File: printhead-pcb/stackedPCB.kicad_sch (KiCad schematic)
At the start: 5 parts, among them J3 Conn_02x08_Row_Letter_Last

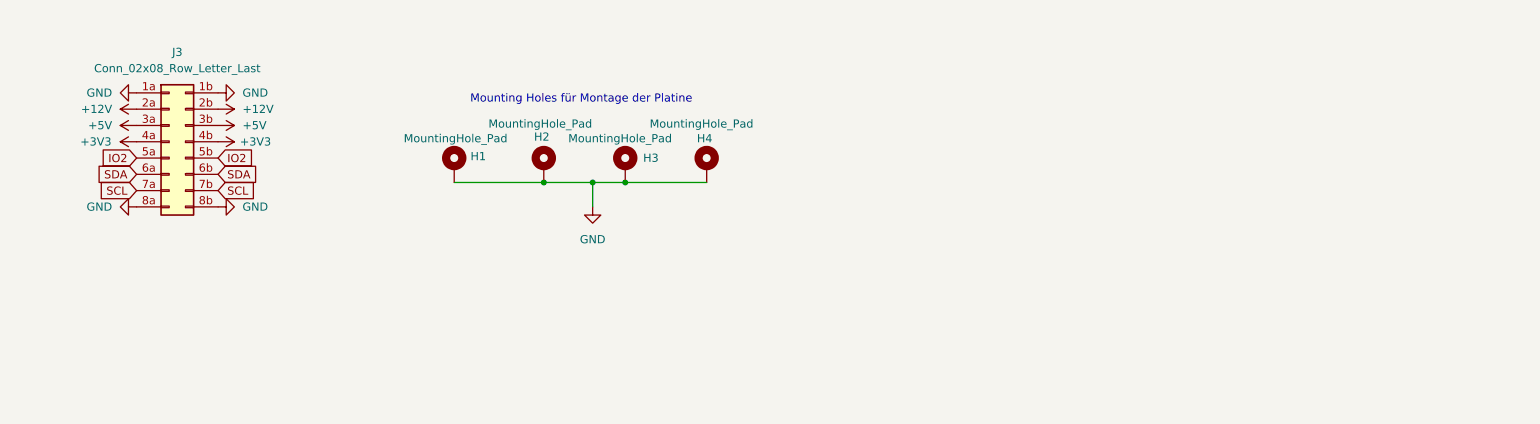
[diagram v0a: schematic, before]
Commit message: made first pcb design of module 1 with components on front and back
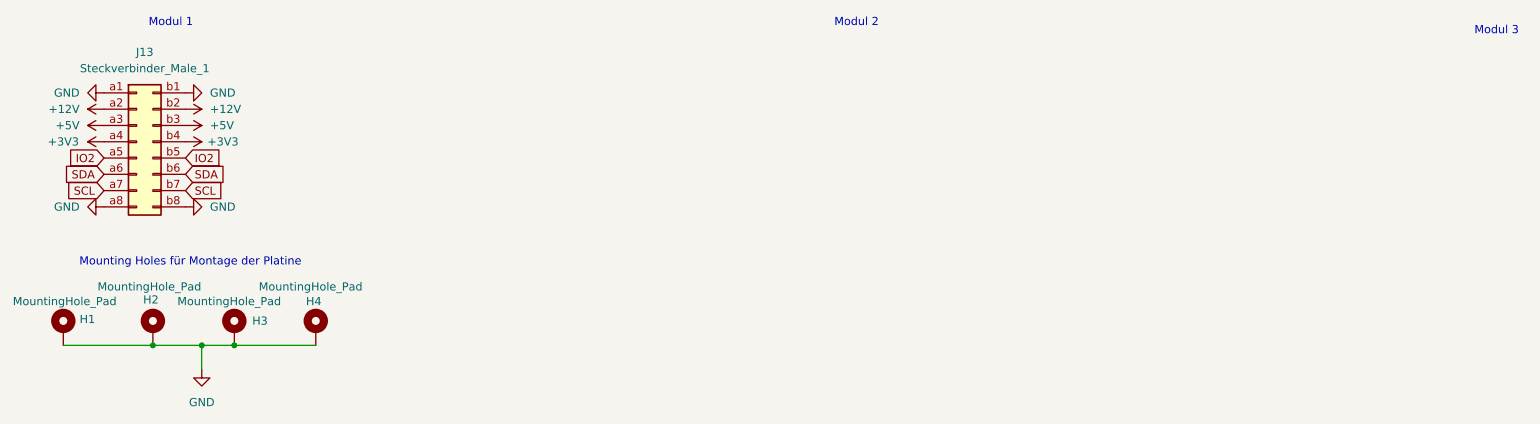
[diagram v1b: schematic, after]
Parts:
- removed J3: Conn_02x08_Row_Letter_Last, symbol Connector_Generic:Conn_02x08_Row_Letter_Last
- added J13: Steckverbinder_Male_1, CustomFotLibByJan:BF100-16-A-D-1-0640-L-C, symbol Connector_Generic:Conn_02x08_Row_Letter_First
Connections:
- net +12V: now also J13.a2 (Pin_a2), J13.b2 (Pin_b2)
- net +3V3: now also J13.a4 (Pin_a4), J13.b4 (Pin_b4)
- net +5V: now also J13.a3 (Pin_a3), J13.b3 (Pin_b3)
- net GND: now also J13.a1 (Pin_a1), J13.a8 (Pin_a8), J13.b1 (Pin_b1), J13.b8 (Pin_b8)
- net IO2: now also J13.a5 (Pin_a5), J13.b5 (Pin_b5)
- net SCL: now also J13.a7 (Pin_a7), J13.b7 (Pin_b7)
- net SDA: now also J13.a6 (Pin_a6), J13.b6 (Pin_b6)
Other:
- note added: "Modul 1"
- note added: "Modul 2"
- note added: "Modul 3"
- moved on the sheet: H1, H2, H3, H4

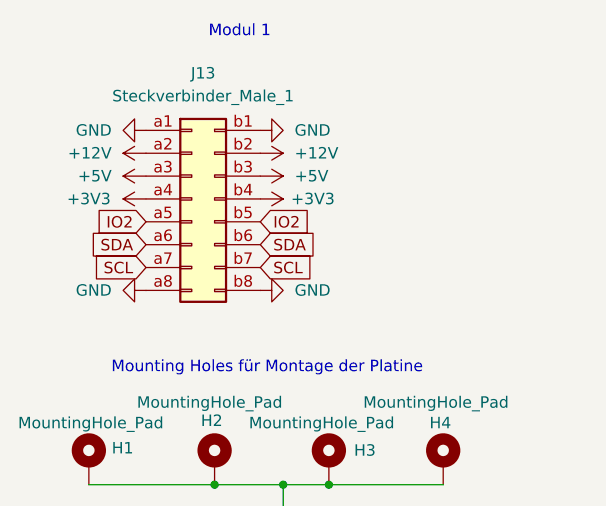
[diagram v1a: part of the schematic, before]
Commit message: alle module mal grob gemacht, beim ersten noch den gpio hinzugefuegt, leider nicht auf einer layerseite untergebracht
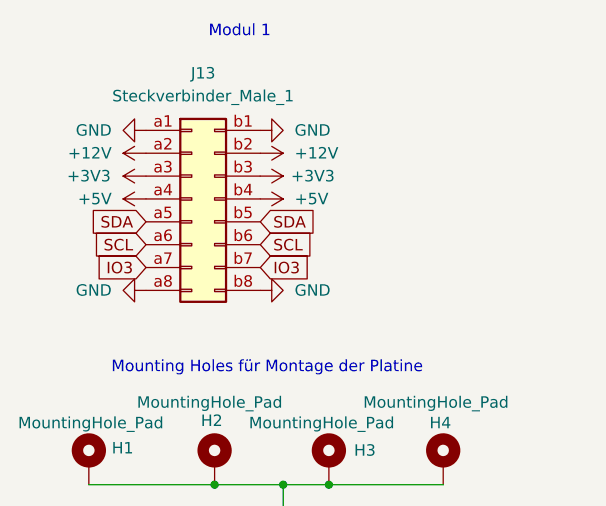
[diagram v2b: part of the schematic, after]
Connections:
- net IO2 is gone; now on net SDA: J13.a5 (Pin_a5), J13.b5 (Pin_b5)
- net +3V3: now also J13.a3 (Pin_a3), J13.b3 (Pin_b3); no longer J13.a4 (Pin_a4), J13.b4 (Pin_b4)
- net +5V: now also J13.a4 (Pin_a4), J13.b4 (Pin_b4); no longer J13.a3 (Pin_a3), J13.b3 (Pin_b3)
- net SCL: now also J13.a6 (Pin_a6), J13.b6 (Pin_b6); no longer J13.a7 (Pin_a7), J13.b7 (Pin_b7)
- net SDA: no longer J13.a6 (Pin_a6), J13.b6 (Pin_b6)
- new net IO3: J13.a7 (Pin_a7), J13.b7 (Pin_b7)

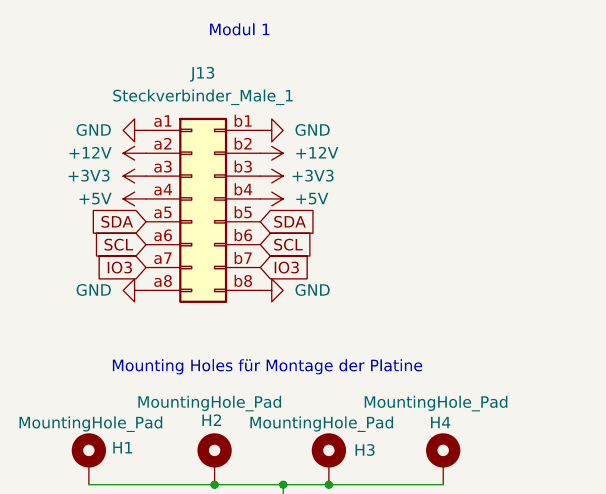
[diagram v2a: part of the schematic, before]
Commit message: working, good version with one layer and equally long signal routes, thicker traces and fitting text
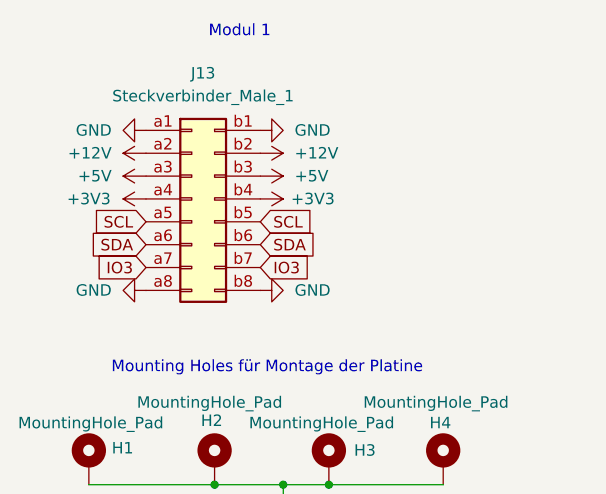
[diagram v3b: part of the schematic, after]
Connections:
- net +3V3: now also J13.a4 (Pin_a4), J13.b4 (Pin_b4); no longer J13.a3 (Pin_a3), J13.b3 (Pin_b3)
- net +5V: now also J13.a3 (Pin_a3), J13.b3 (Pin_b3); no longer J13.a4 (Pin_a4), J13.b4 (Pin_b4)
- net SCL: now also J13.a5 (Pin_a5), J13.b5 (Pin_b5); no longer J13.a6 (Pin_a6), J13.b6 (Pin_b6)
- net SDA: now also J13.a6 (Pin_a6), J13.b6 (Pin_b6); no longer J13.a5 (Pin_a5), J13.b5 (Pin_b5)

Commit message: prepared second module for tomorrow
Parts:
- added H5, H6, H7, H8: MountingHole_Pad, MountingHole:MountingHole_2.2mm_M2_Pad_TopBottom, symbol Mechanical:MountingHole_Pad
- added J14: Steckverbinder_Male_2, CustomFotLibByJan:BF100-16-A-D-1-0640-L-C, symbol Connector_Generic:Conn_02x08_Row_Letter_First
- added J15: Steckverbinder_Female_2, CustomFotLibByJan:BF100-16-A-D-1-0640-L-C, symbol Connector_Generic:Conn_02x08_Row_Letter_First
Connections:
- net +12V: now also J14.a2 (Pin_a2), J14.b2 (Pin_b2), J15.a2 (Pin_a2), J15.b2 (Pin_b2)
- net +3V3: now also J14.a4 (Pin_a4), J14.b4 (Pin_b4), J15.a4 (Pin_a4), J15.b4 (Pin_b4)
- net +5V: now also J14.a3 (Pin_a3), J14.b3 (Pin_b3), J15.a3 (Pin_a3), J15.b3 (Pin_b3)
- net GND: now also H5.1, H6.1, H7.1, H8.1, J14.a1 (Pin_a1), J14.a8 (Pin_a8), J14.b1 (Pin_b1), J14.b8 (Pin_b8), J15.a1 (Pin_a1), J15.a8 (Pin_a8), J15.b1 (Pin_b1), J15.b8 (Pin_b8)
- net IO3: now also J14.a7 (Pin_a7), J14.b7 (Pin_b7), J15.a7 (Pin_a7), J15.b7 (Pin_b7)
- net SCL: now also J14.a5 (Pin_a5), J14.b5 (Pin_b5), J15.a5 (Pin_a5), J15.b5 (Pin_b5)
- net SDA: now also J14.a6 (Pin_a6), J14.b6 (Pin_b6), J15.a6 (Pin_a6), J15.b6 (Pin_b6)

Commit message: refractoring
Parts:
- H1, H2, H3, H4, H5, H6, H7, H8: value MountingHole_Pad -> MountHole
- J15: footprint CustomFotLibByJan:BF100-16-A-D-1-0640-L-C -> CustomFotLibByJan:BF030-16A-B1-0360-0277-0600-LB
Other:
- moved on the sheet: J14, J15

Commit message: unsaved changes
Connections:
- net +12V: now also J15.a7 (Pin_a7), J15.b7 (Pin_b7); no longer J15.a2 (Pin_a2), J15.b2 (Pin_b2)
- net +3V3: now also J15.a5 (Pin_a5), J15.b5 (Pin_b5); no longer J15.a4 (Pin_a4), J15.b4 (Pin_b4)
- net +5V: now also J15.a6 (Pin_a6), J15.b6 (Pin_b6); no longer J15.a3 (Pin_a3), J15.b3 (Pin_b3)
- net IO3: now also J15.a2 (Pin_a2), J15.b2 (Pin_b2); no longer J15.a7 (Pin_a7), J15.b7 (Pin_b7)
- net SCL: now also J15.a4 (Pin_a4), J15.b4 (Pin_b4); no longer J15.a5 (Pin_a5), J15.b5 (Pin_b5)
- net SDA: now also J15.a3 (Pin_a3), J15.b3 (Pin_b3); no longer J15.a6 (Pin_a6), J15.b6 (Pin_b6)

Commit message: played around with nets and net classes
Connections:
- net IO3 is gone; now on net +12V: J13.a7 (Pin_a7), J13.b7 (Pin_b7), J14.a7 (Pin_a7), J14.b7 (Pin_b7), J15.a2 (Pin_a2), J15.b2 (Pin_b2)
- net SCL is gone; now on net +3V3: J13.a5 (Pin_a5), J13.b5 (Pin_b5), J14.a5 (Pin_a5), J14.b5 (Pin_b5), J15.a4 (Pin_a4), J15.b4 (Pin_b4)
- net SDA is gone; now on net +5V: J13.a6 (Pin_a6), J13.b6 (Pin_b6), J14.a6 (Pin_a6), J14.b6 (Pin_b6), J15.a3 (Pin_a3), J15.b3 (Pin_b3)
